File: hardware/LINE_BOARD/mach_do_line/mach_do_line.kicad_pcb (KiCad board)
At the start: 2 copper layers, 52 x 17 mm, 33 parts, among them J10 Conn_01x01_Pin, J11 Conn_01x01_Pin, J12 Conn_01x01_Pin, J18 Conn_01x01_Pin, J2 Conn_01x01_Pin

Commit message: add pcb line
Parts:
- moved R5 0.71 mm to (40.5, 45.8)
- moved R16 0.32 mm to (87.7, 45.9)
- moved R17 0.32 mm to (87.7, 49.3)
- renumbered +5V to 5V
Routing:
- net /s3: track 18.9 -> 15.7 mm
- net +3V3: track 91.7 -> 94.0 mm, vias 2 -> 0
- net /s4: track 18.9 -> 20.4 mm
- net /s1: track 18.1 -> 18.9 mm
- net Net-(U2-E): track 2.49 -> 1.78 mm
- net +5V: track 49.1 -> 48.9 mm, vias 9 -> 6
- net GND: vias 19 -> 0
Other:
- board text added: "."
- board text added: "S2"
- board text added: "S3"
- board text added: "S4"
- board text added: "S5"

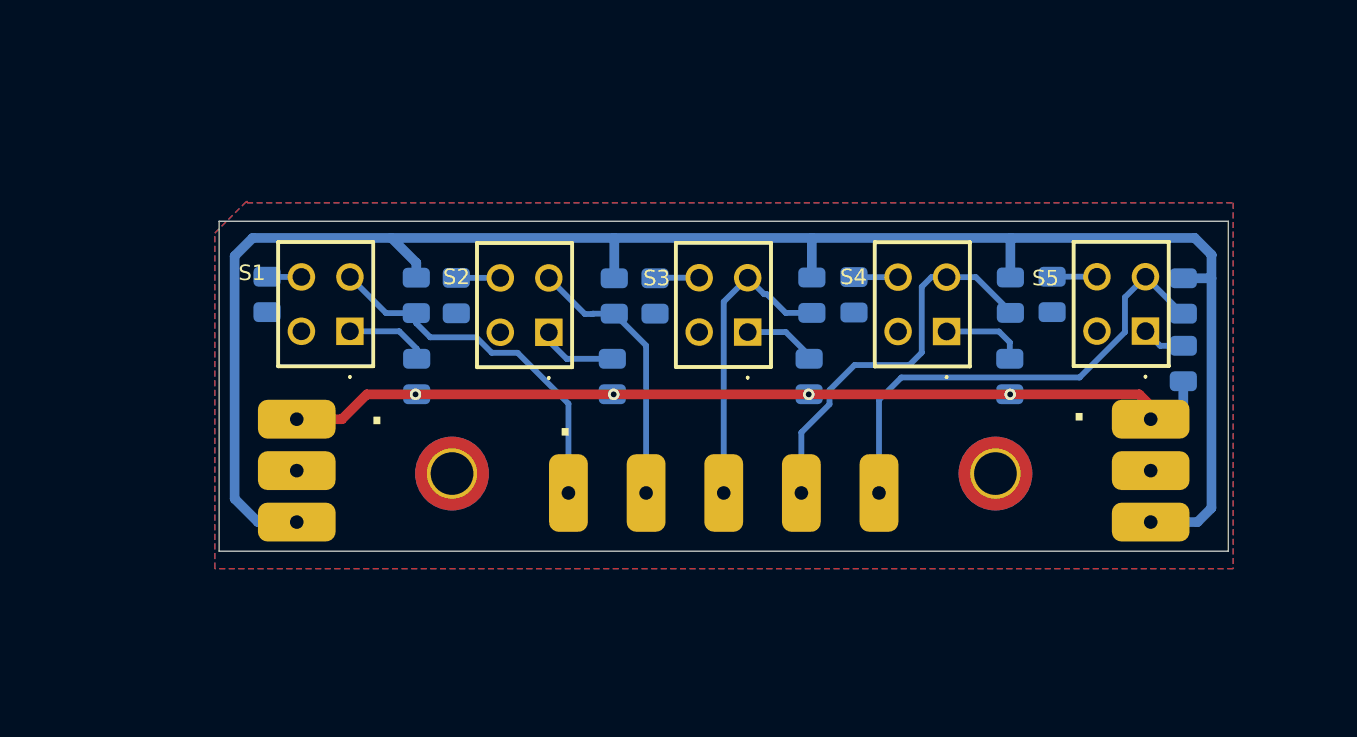
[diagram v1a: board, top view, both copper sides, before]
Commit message: add pcb line 15mm, 10mm
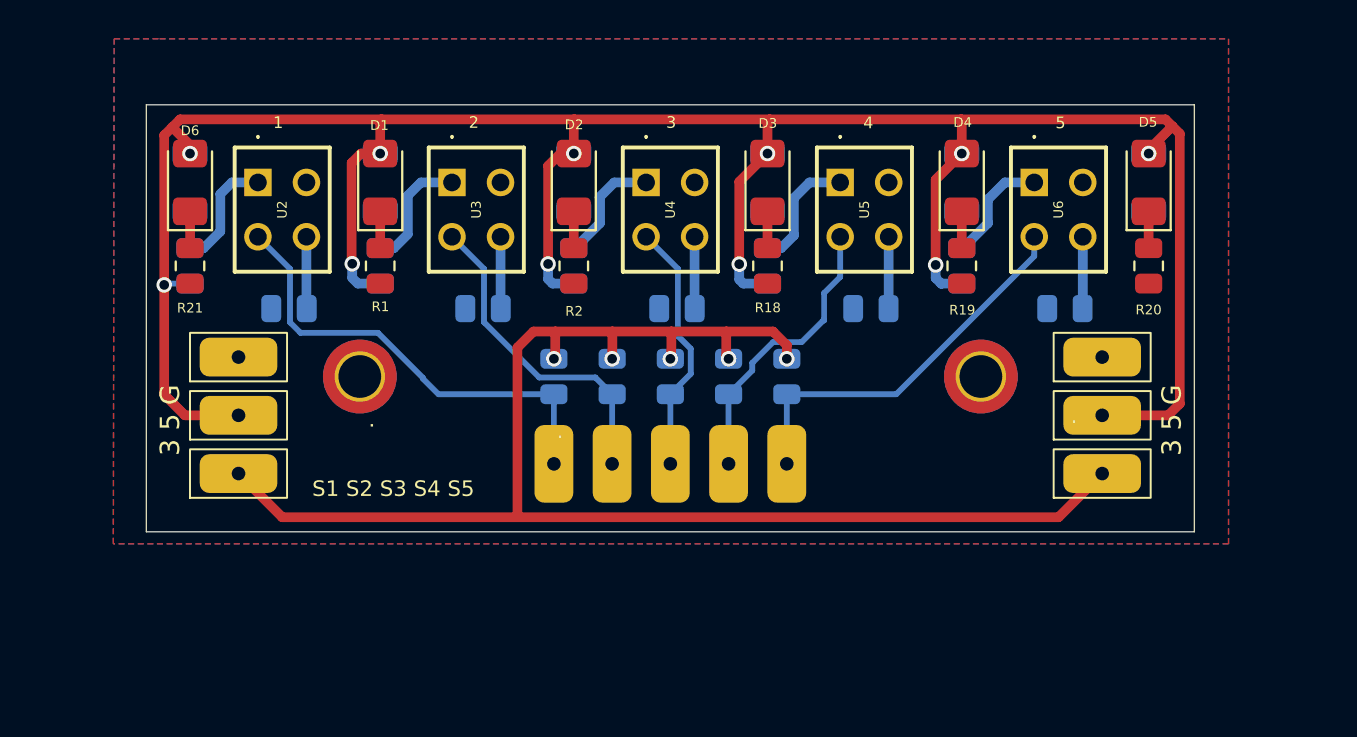
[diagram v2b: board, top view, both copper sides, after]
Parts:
- removed 3V3 (x2), 5V (x2), GND (x2): Conn_01x01_Pin, SolderPAD-2x4mm:PAD-2x4mm-SMD
- removed S1, S2, S3, S4, S5: RPR-220, RPR220:RPR220
- added C1: 100uF, Capacitor_SMD:C_1206_3216Metric, B.Cu at (36.5, 40.0)
- added C2: 100uF, Capacitor_SMD:C_1206_3216Metric, B.Cu at (46.3, 40.0)
- added C3: 100uF, Capacitor_SMD:C_1206_3216Metric, B.Cu at (56.3, 40.0)
- added C4: 100uF, Capacitor_SMD:C_1206_3216Metric, B.Cu at (66.3, 40.0)
- added C5: 100uF, Capacitor_SMD:C_1206_3216Metric, B.Cu at (76.3, 40.0)
- added C6: 100uF, Capacitor_SMD:C_1206_3216Metric, B.Cu at (85.9, 40.0)
- added D1: LED_Small, LED_SMD:LED_1206_3216Metric_Pad1.42x1.75mm_HandSolder, F.Cu at (46.3, 40.0)
- added D2: LED_Small, LED_SMD:LED_1206_3216Metric_Pad1.42x1.75mm_HandSolder, F.Cu at (56.3, 40.0)
- added D3: LED_Small, LED_SMD:LED_1206_3216Metric_Pad1.42x1.75mm_HandSolder, F.Cu at (66.3, 40.0)
- added D4: LED_Small, LED_SMD:LED_1206_3216Metric_Pad1.42x1.75mm_HandSolder, F.Cu at (76.3, 40.0)
- added D5: LED_Small, LED_SMD:LED_1206_3216Metric_Pad1.42x1.75mm_HandSolder, F.Cu at (85.9, 40.0)
- added D6: LED_Small, LED_SMD:LED_1206_3216Metric_Pad1.42x1.75mm_HandSolder, F.Cu at (36.5, 40.0)
- added J13: Conn_01x01_Pin, SolderPAD-2x4mm:PAD-2x4mm-SMD, F.Cu at (39.0, 52.0)
- added J14: Conn_01x01_Pin, SolderPAD-2x4mm:PAD-2x4mm-SMD, F.Cu at (39.0, 49.0)
- added J15: Conn_01x01_Pin, SolderPAD-2x4mm:PAD-2x4mm-SMD, F.Cu at (83.5, 55.0)
- added J16: Conn_01x01_Pin, SolderPAD-2x4mm:PAD-2x4mm-SMD, F.Cu at (83.5, 52.0)
- added J17: Conn_01x01_Pin, SolderPAD-2x4mm:PAD-2x4mm-SMD, F.Cu at (83.5, 49.0)
- added J3: Conn_01x01_Pin, SolderPAD-2x4mm:PAD-2x4mm-SMD, F.Cu at (39.0, 55.0)
- added R1: 220, Resistor_SMD:R_0805_2012Metric, F.Cu at (46.3, 44.3)
- added R18: 220, Resistor_SMD:R_0805_2012Metric, F.Cu at (66.3, 44.3)
- added R19: 220, Resistor_SMD:R_0805_2012Metric, F.Cu at (76.3, 44.3)
- added R2: 220, Resistor_SMD:R_0805_2012Metric, F.Cu at (56.3, 44.3)
- added R20: 220, Resistor_SMD:R_0805_2012Metric, F.Cu at (85.9, 44.3)
- added R21: 220, Resistor_SMD:R_0805_2012Metric, F.Cu at (36.5, 44.3)
- added U2: RPR-220, RPR-220:RPR220, F.Cu at (40.0, 40.0)
- added U3: RPR-220, RPR-220:RPR220, F.Cu at (50.0, 40.0)
- added U4: RPR-220, RPR-220:RPR220, F.Cu at (60.0, 40.0)
- added U5: RPR-220, RPR-220:RPR220, F.Cu at (70.0, 40.0)
- added U6: RPR-220, RPR-220:RPR220, F.Cu at (80.0, 40.0)
- moved R16 20.8 mm to (67.2, 50.0)
- moved R13 15.1 mm to (64.2, 50.0)
- moved R14 13.7 mm to (66.3, 44.3)
- moved R11 13.4 mm to (56.3, 44.3)
- moved R8 13.2 mm to (46.3, 44.3)
- moved R3 13.0 mm to (36.5, 44.3)
- moved R17 12.5 mm to (76.3, 44.3)
- moved R10 8.41 mm to (61.2, 50.0)
- moved R4 8.23 mm to (55.2, 50.0)
- moved H1 6.90 mm to (45.2, 50.0)
- moved H2 5.06 mm to (77.2, 50.0)
- moved J18 4.98 mm to (67.2, 54.5)
- moved R7 4.15 mm to (58.2, 50.0)
- moved J12 4.04 mm to (64.2, 54.5)
- moved J11 3.13 mm to (61.2, 54.5)
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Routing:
- net +5V: track 48.9 -> 136.0 mm, vias 6 -> 11
- net +3V3: track 94.0 -> 76.1 mm, vias 0 -> 5
- net /s4: track 20.4 -> 15.0 mm
- net /s1: track 18.9 -> 23.8 mm
- net /s5: track 24.9 -> 20.3 mm
- net Net-(U6-A): track 2.26 -> 5.87 mm
- net /s2: track 14.1 -> 16.8 mm
- net /s3: track 15.7 -> 13.1 mm
- net Net-(U3-A): track 4.11 -> 6.27 mm
- net Net-(U4-A): track 3.84 -> 5.95 mm
- net Net-(U5-A): track 4.34 -> 6.27 mm
- net Net-(U2-E): track 1.78 -> 3.71 mm
- net Net-(D6-K): track 0.00 -> 1.90 mm
- net Net-(D5-K): track 0.00 -> 1.90 mm
- net Net-(D4-K): track 0.00 -> 1.90 mm
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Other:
- board size 52 x 17 mm -> 54 x 22 mm
- board text added: "1"
- board text added: "2"
- board text added: "3"
- board text added: "3 5 G"
- board text added: "4"
- board text added: "5"
- board text added: "S1 S2 S3 S4 S5"
